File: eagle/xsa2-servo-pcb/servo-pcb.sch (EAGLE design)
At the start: 44 parts, among them IC1 ESP32-WROOM-32D__4MB_PS_, IC2 FT231XS-R, IC3 NJM2884U1-33-TE1, IC4 TPA2006D1DRBR, IC5 ISL90728UIE627Z-TK, J1 WJEK254-2.54-02P-140-00A, J3 WJEK254-2.54-02P-140-00A, J4 WJEK254-2.54-02P-140-00A, Q1 IRLML6402, Q2 2SC2712-GR_F_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

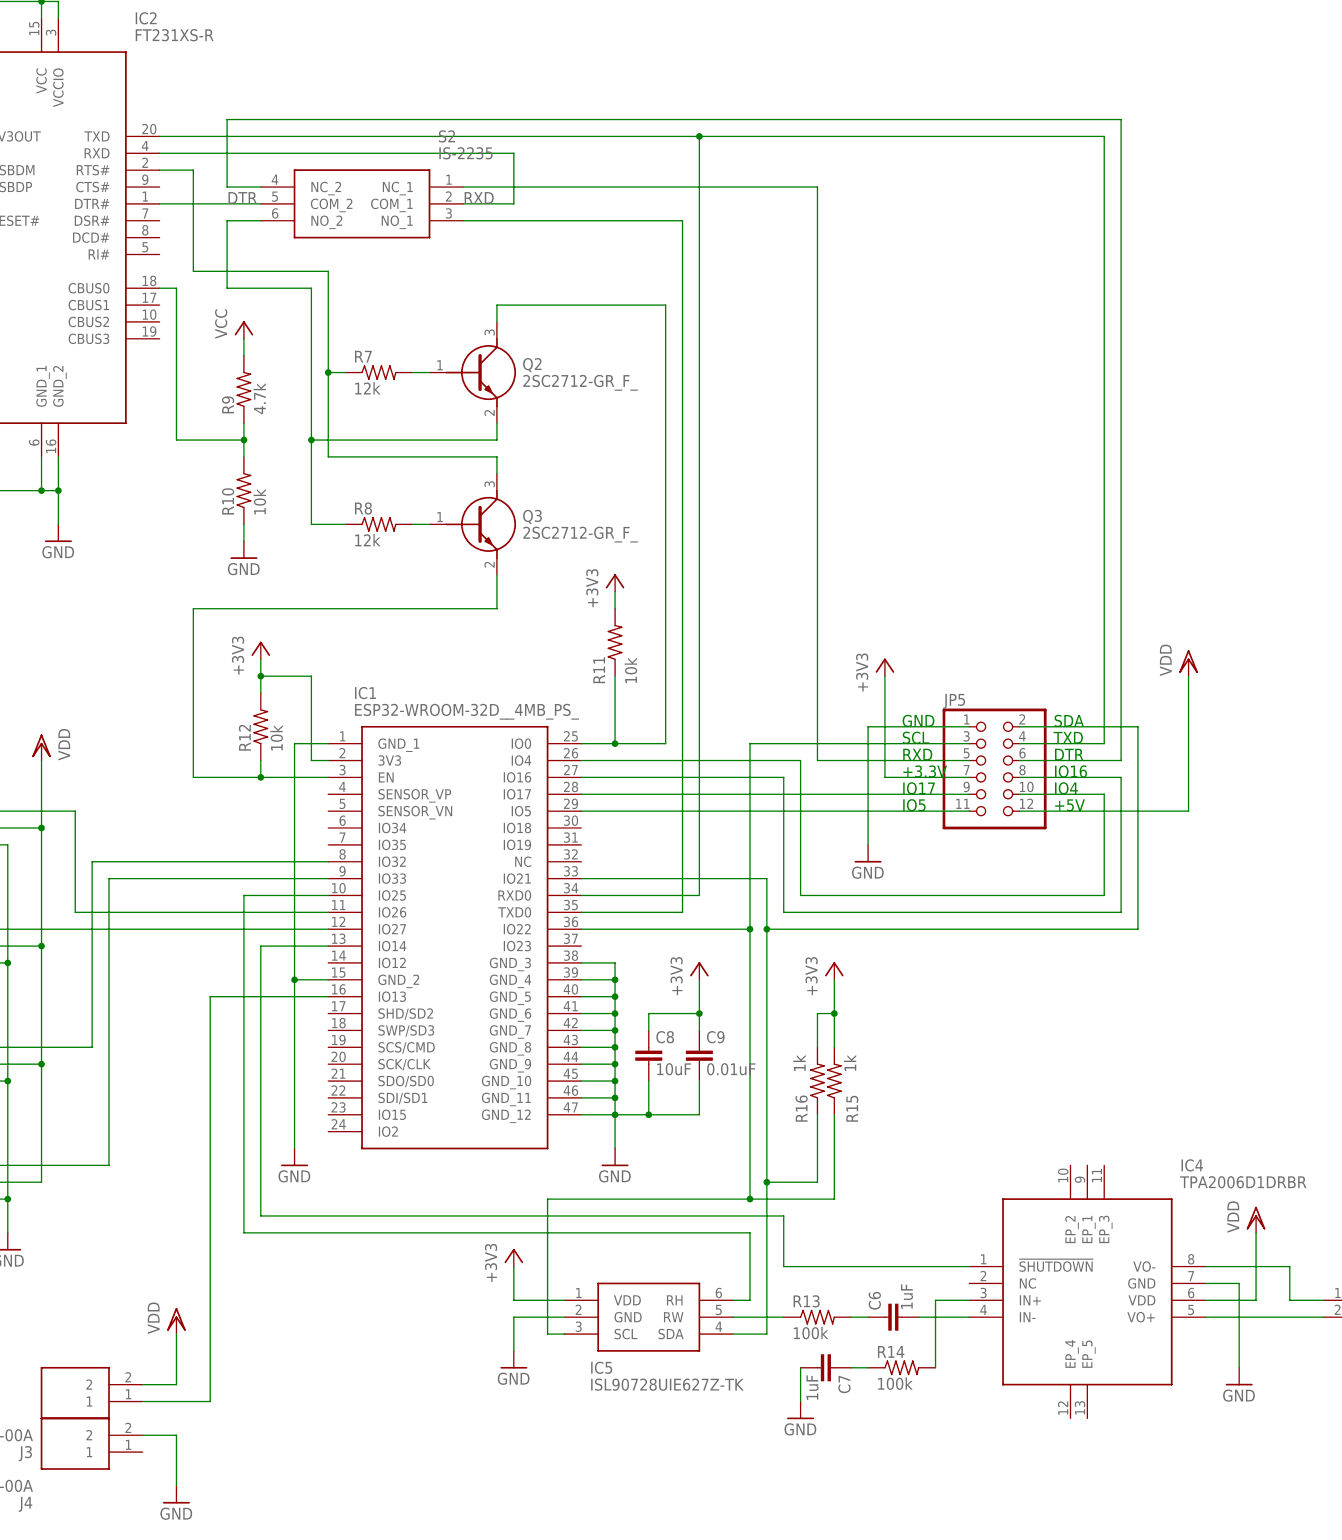
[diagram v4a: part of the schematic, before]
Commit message: [eagle] 連結コネクタのピン数を増加
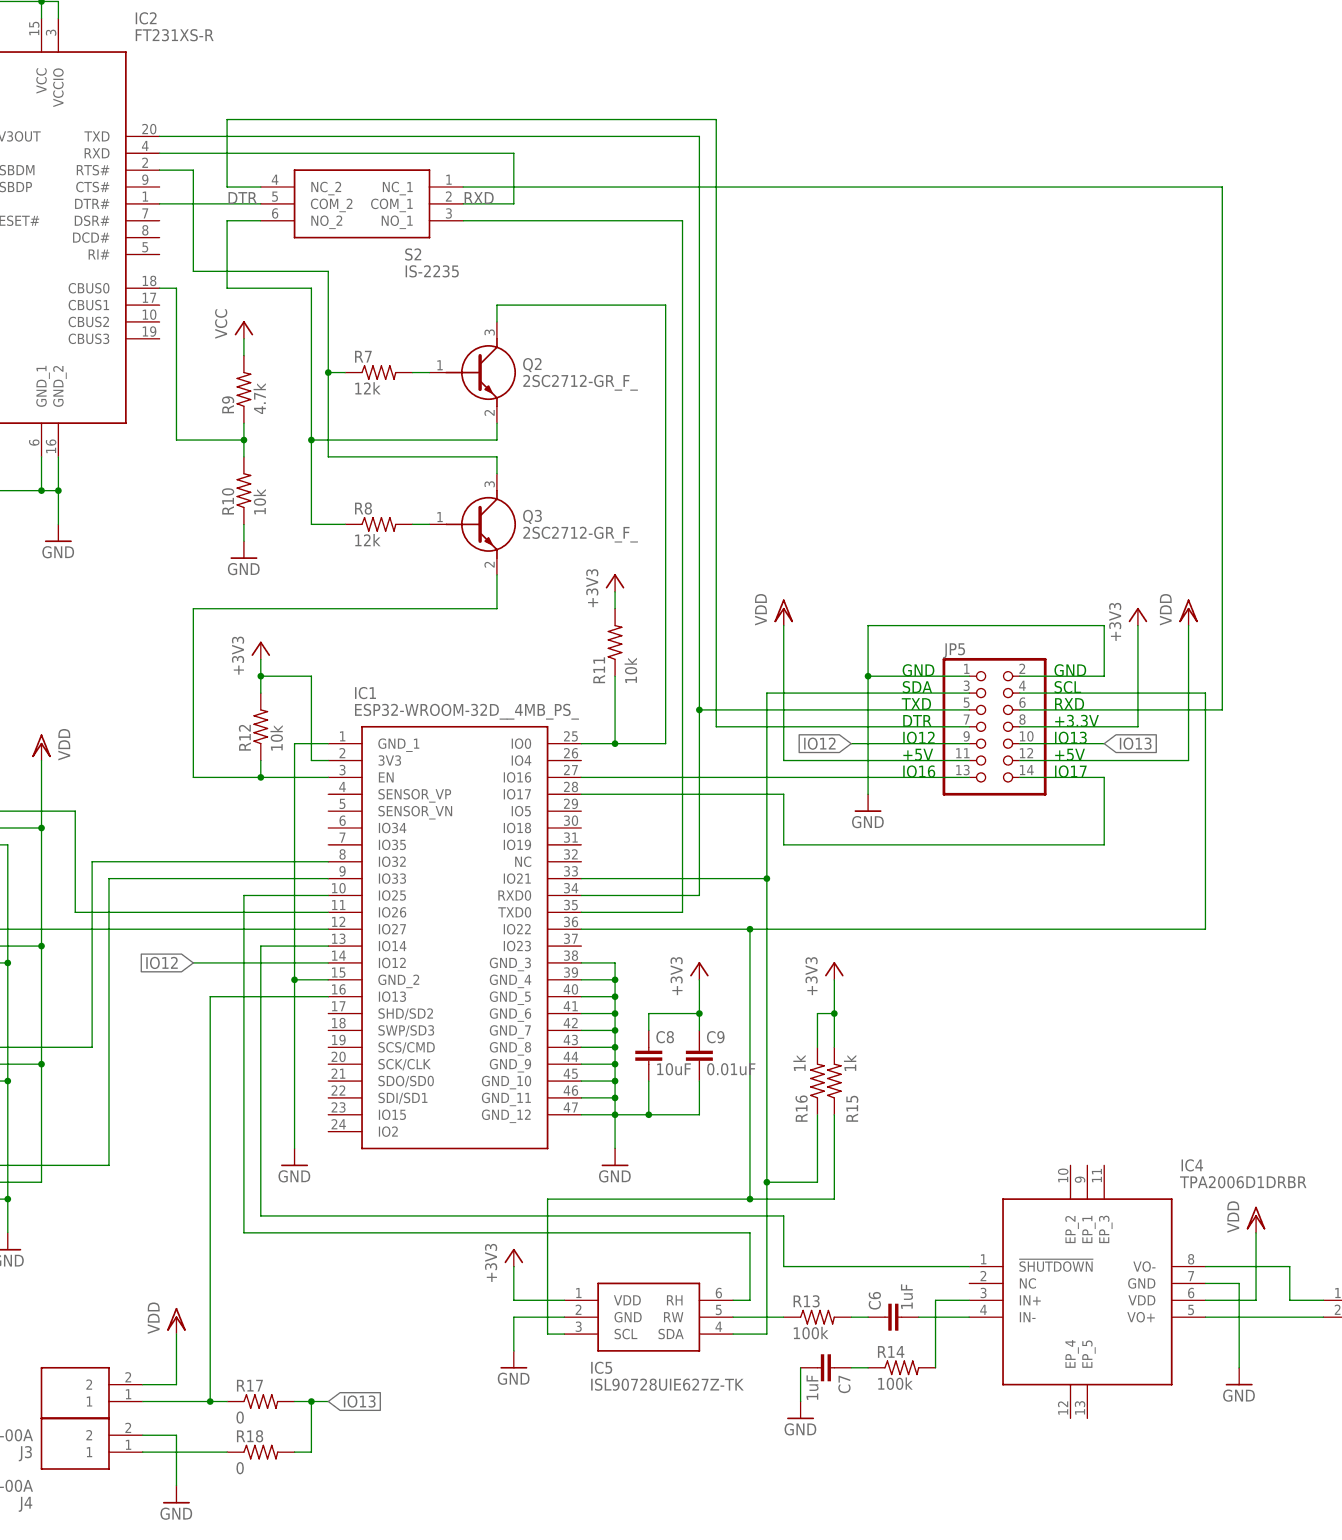
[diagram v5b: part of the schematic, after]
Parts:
- added R17, R18: 0, rcl:R-US_R0603
- JP1, JP2, JP3, JP4: device pinhead:PINHD-1X3/90 -> pinhead:PINHD-1X3
- JP5: device pinhead:PINHD-2X6 -> pinhead:PINHD-2X7
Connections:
- removed net N$37: IC1.IO4, JP5.10
- removed net N$38: IC1.IO5, JP5.11
- removed net N$40: IC1.RXD0, IC2.TXD, JP5.4
- new net IO12: IC1.IO12, JP5.9
- new net IO13: JP5.10, R17.2, R18.2
- new net N$4: IC1.IO17, JP5.14
- new net N$6: IC1.RXD0, IC2.TXD, JP5.5
- net +3V3: now also JP5.8; no longer JP5.7
- net GND: now also JP5.2
- net N$17: now also JP5.7; no longer JP5.6
- net N$23: now also JP5.4; no longer JP5.3
- net N$24: now also JP5.3; no longer JP5.2
- net N$29: now also R17.1
- net N$34: now also JP5.13; no longer JP5.8
- net N$36: now also J4.1, R18.1; no longer IC1.IO17, JP5.9
- net N$41: now also JP5.6; no longer JP5.5
- net VDD: now also JP5.11
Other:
- note added: "IO12"
- note added: "IO13"
- note removed: "IO4"
- note removed: "IO5"

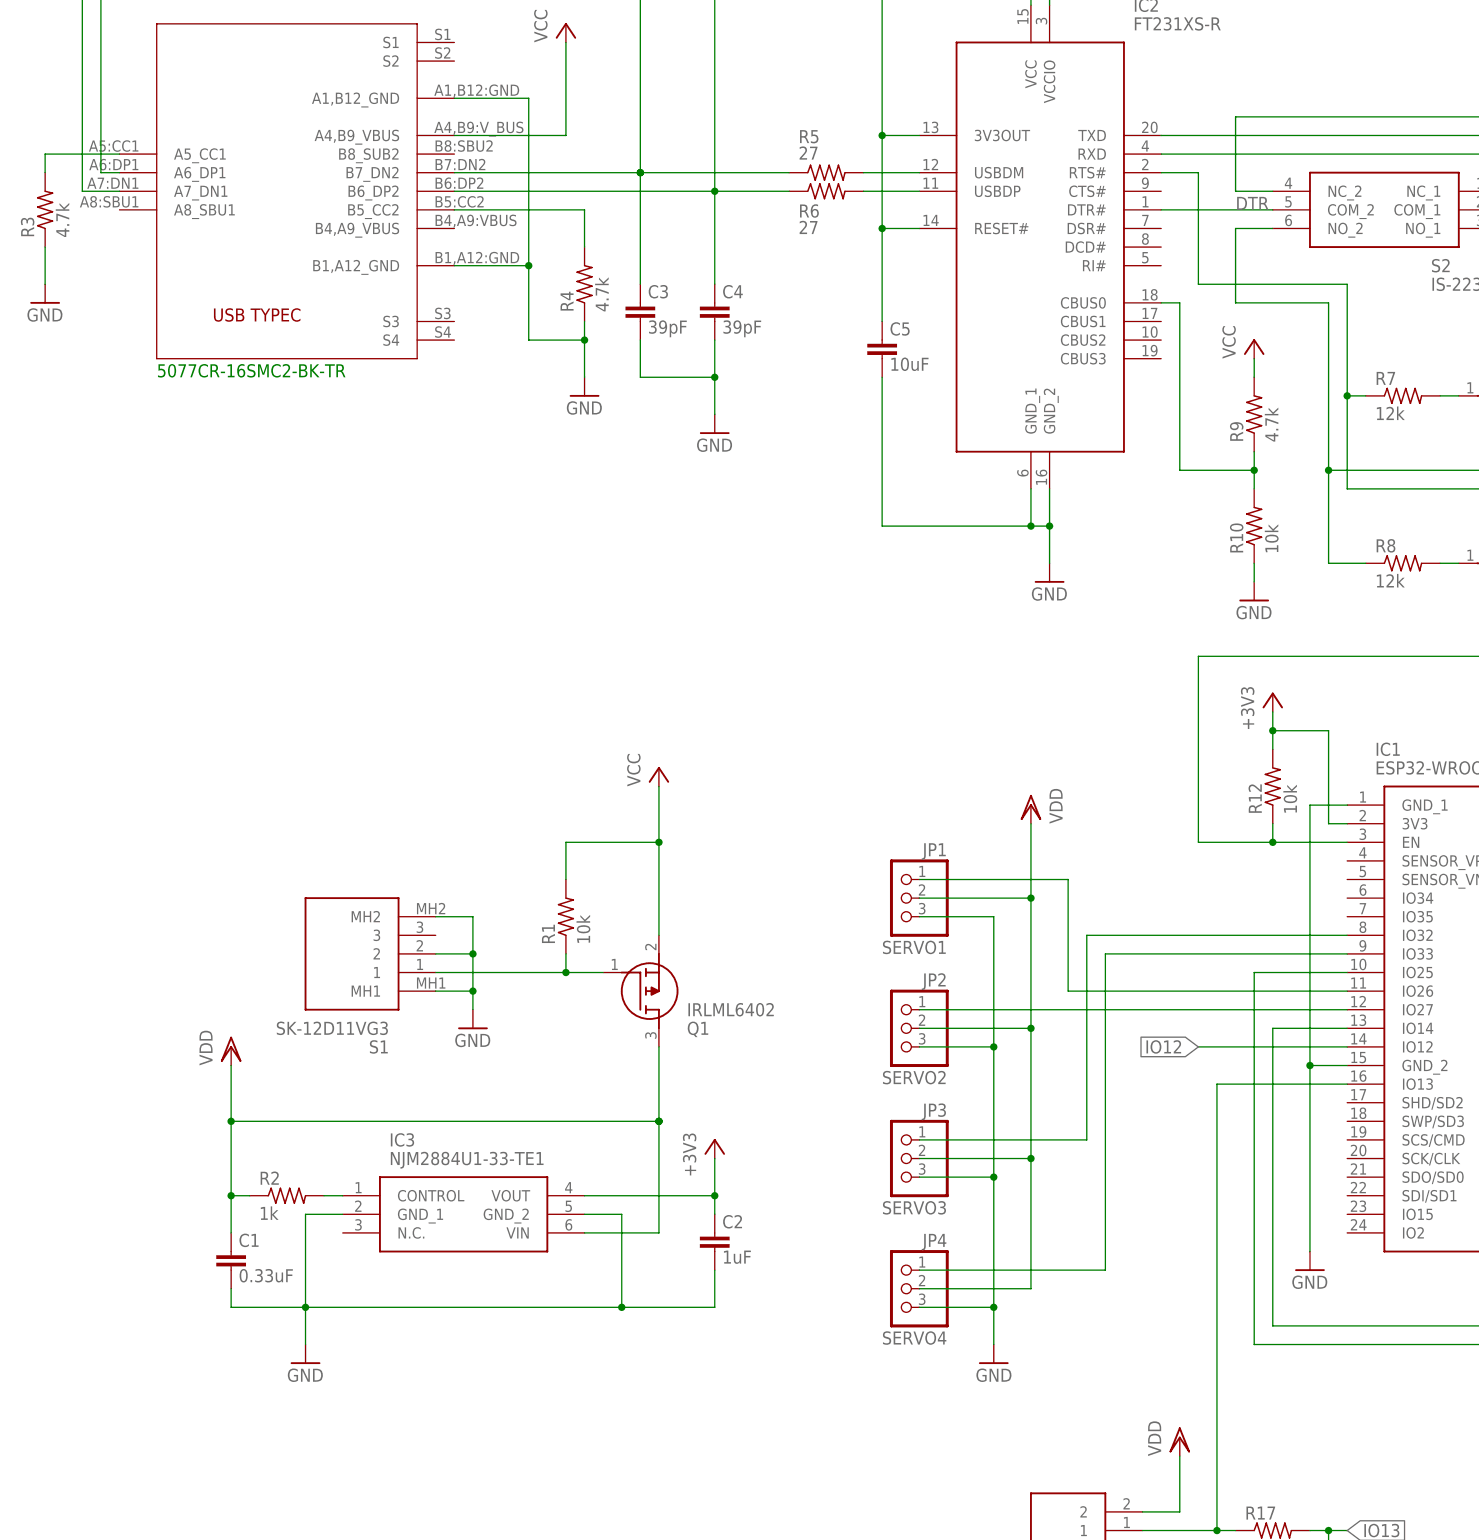
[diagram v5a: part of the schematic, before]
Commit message: [eagle] パターン追加
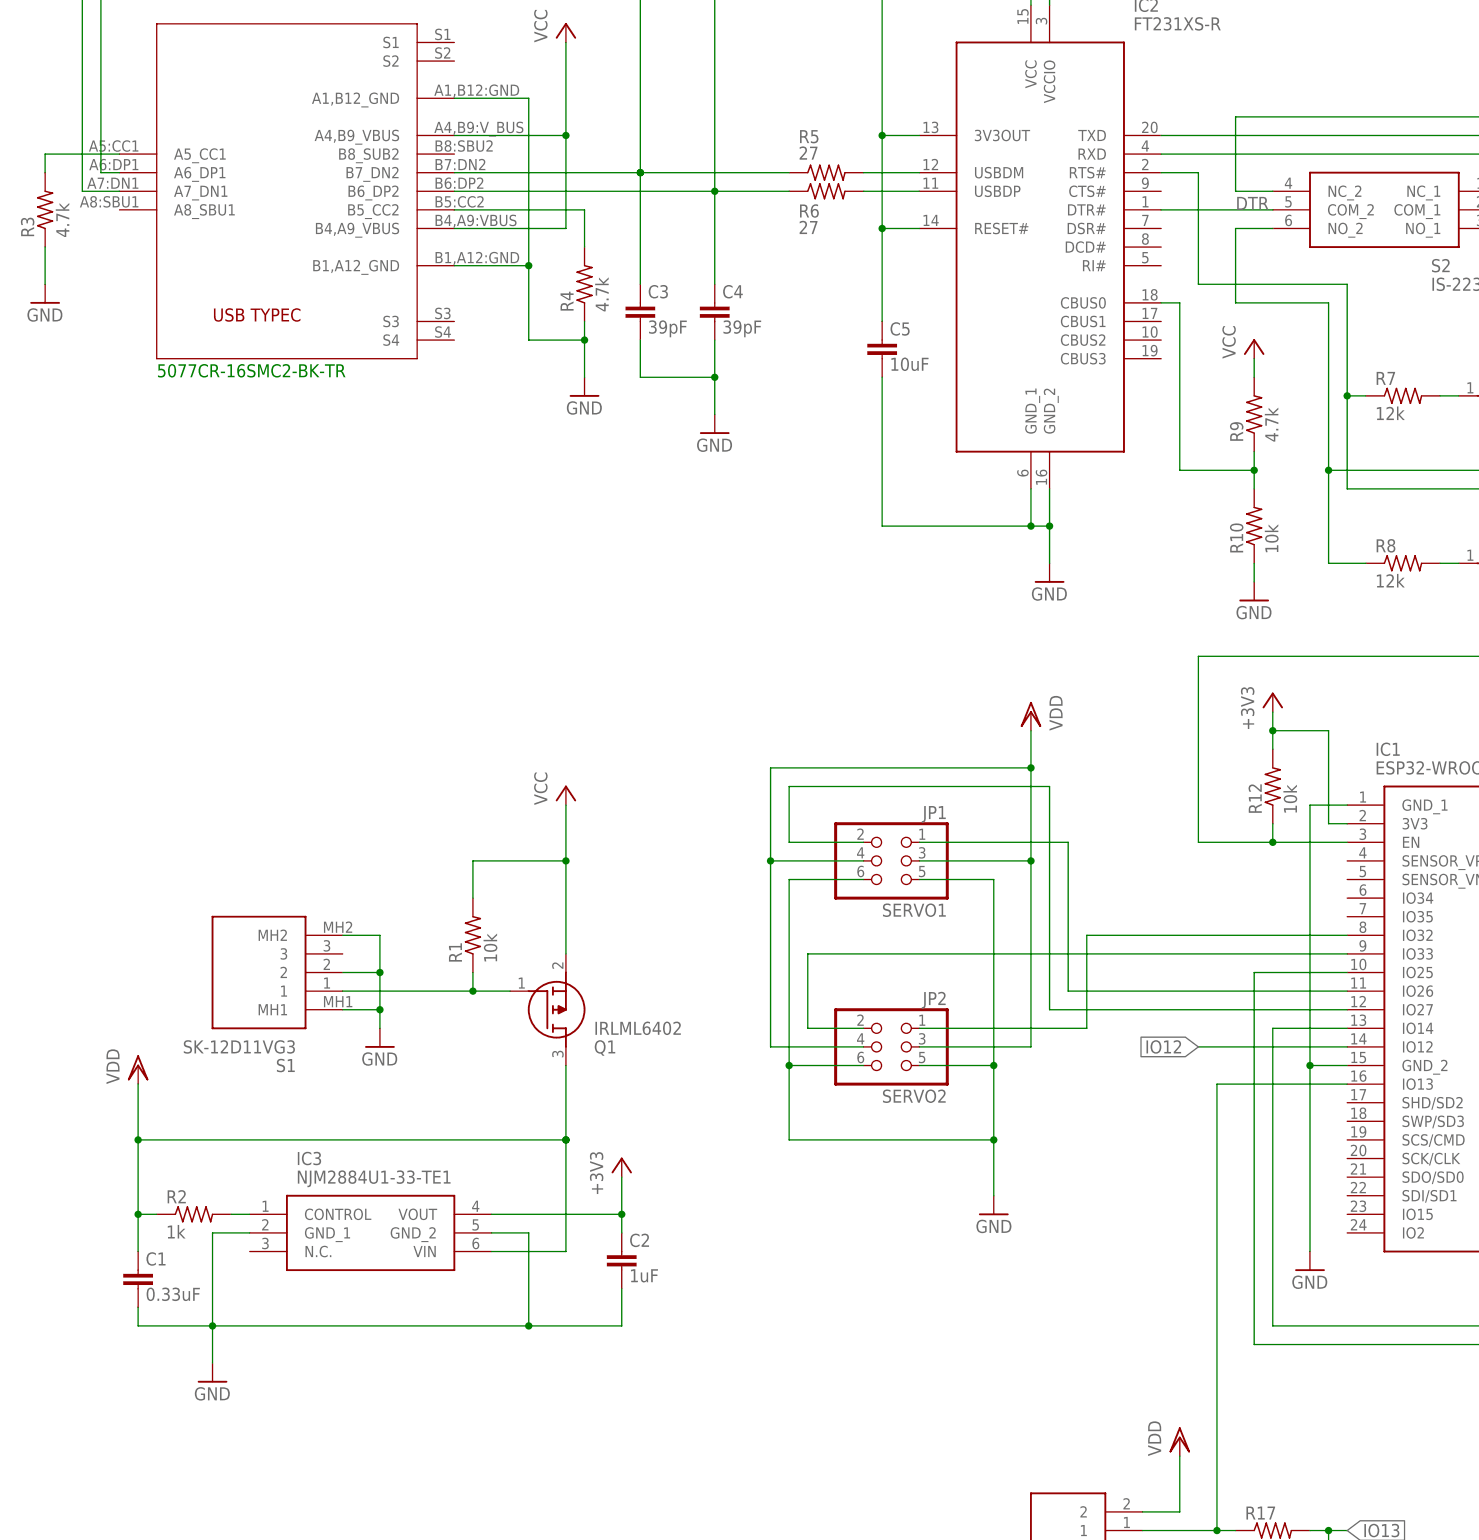
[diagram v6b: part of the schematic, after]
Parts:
- removed JP3: SERVO3, pinhead:PINHD-1X3
- removed JP4: SERVO4, pinhead:PINHD-1X3
- C5, C8: device rcl:C-EUC0603 -> rcl:C-EUC0805
- JP1, JP2: device pinhead:PINHD-1X3 -> pinhead:PINHD-2X3/90
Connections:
- net GND: now also JP1.5, JP1.6, JP2.5, JP2.6; no longer JP1.3, JP2.3, JP3.3, JP4.3
- net N$31: now also JP1.2; no longer JP2.1
- net N$32: now also JP2.1; no longer JP3.1
- net N$33: now also JP2.2; no longer JP4.1
- net VCC: now also U$1.B4,A9_VBUS
- net VDD: now also JP1.3, JP1.4, JP2.3, JP2.4; no longer JP1.2, JP2.2, JP3.2, JP4.2
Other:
- moved on the sheet: C1, C2, IC3, Q1, R1, R2, S1

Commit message: [eagle] サーボ基板完成
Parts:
- added FL1: BLM18PG121SN1D, SamacSys_Parts:BLM18PG121SN1D
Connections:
- new net N$38: FL1.1, JP1.3, JP1.4, JP2.3, JP2.4
- net VDD: now also FL1.2; no longer JP1.3, JP1.4, JP2.3, JP2.4
